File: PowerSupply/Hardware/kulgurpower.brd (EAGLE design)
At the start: 102 x 86.5 mm, 97 parts, among them X2 1727036

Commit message: Lot of changes to schematics. A lot.
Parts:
- removed E-STOP: PC-6-16/2-G-10.16-1913646, phoenix-1016:PC-6-16/2-G-10.16
- removed PWR1, PWR2, PWR3, PWR4: MST2V, con-phoenix-508:MSTBV2
- removed R10, R14, R3, R5: 100k, rcl:R0603
- removed R4: 680k, rcl:R0603
- removed SV2: (no value), con-lstb:MA20-2
- removed TP13: TPB2,54, testpad:B2,54
- added C22, C23, C24, C25, C26, C27, C28: 0.1, rcl:C0603
- added D1, D3: BAT54C, diode:SOT23
- added M1, M2, M3, M4: MST2V, con-phoenix-508:MSTBV2
- added R11, R15, R17, R19: 680k, rcl:R0603
- added R13, R16, R20: 100k, rcl:R0603
- added SV1: (no value), con-lstb:MA17-2
- added U$20, U$21, U$22, U$23, U$24, U$25, U$26: MAX1614EUA, MAX1614EUA:MAX1614EUA
- added U$27: PC-6-16/2-G-10.16-1913646, phoenix-1016:PC-6-16/2-G-10.16
- C12, C19, C6: device resistor:C0603@1 -> rcl:C0603
- C2: value 0.1 -> 47uF / 10V; device rcl:C0603 -> rcl:C/6032-28R
- C9: device resistor:C0603 -> rcl:C0603
- F1, F10, F2, F3, F4, F5, F6, F7, F8, F9: value PTCSMD -> 10A FUSE 1206
- U$1, U$10, U$12, U$14, U$15, U$2, U$3, U$5, U$6, U$7, U$9: value FDMS8558S -> AON6500
- moved R18 42.9 mm to (59.5, 11.4), turned to 270 degrees
- moved D20 21.0 mm to (94.3, 28.4)
- moved C2 10.8 mm to (33.2, 35.4), turned to 90 degrees
- moved U$2 7.25 mm to (75.0, 26.0)
- moved U$5 7.25 mm to (15.0, 26.0)
- moved U$6 7.25 mm to (55.1, 26.0)
- moved U$9 7.25 mm to (35.0, 26.0)
- moved U$10 6.50 mm to (35.0, 19.2)
- moved U$12 6.50 mm to (15.0, 19.2)
- moved U$3 6.50 mm to (75.0, 19.2)
- moved U$7 6.50 mm to (55.1, 19.2)
- moved PWRLED 6.40 mm to (85.1, 6.10)
- moved R12 6.40 mm to (85.1, 9.76)
- moved C21 6.04 mm to (23.2, 32.0), turned to 90 degrees
- moved F9 6.00 mm to (54.1, 67.8), flipped to the bottom
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- renumbered PWR5 to PC, PWR6 to MISC
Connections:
- removed net EN_OUT1: SV2.16, U$1.P$4
- removed net EN_OUT2: SV2.26, U$14.P$4
- removed net EN_OUT3: SV2.36, U$15.P$4
- removed net N$18 (its old number): L2.1, TP5.TP, U$17.P$4A
- removed net N$2 (its old number): L1.1, TP8.TP, U$16.P$4A
- removed net N$23 (its old number): L3.1, TP10.TP, U$18.P$4A
- removed net N$26: L4.1, TP15.TP, U$19.P$4A
- removed net PBUS1: F10.1, F7.1, F8.1, F9.1, U$1.P$1, U$1.P$2, U$1.P$3
- removed net PBUS2: F1.1, U$14.P$1, U$14.P$2, U$14.P$3
- removed net PBUS3: F2.1, U$15.P$1, U$15.P$2, U$15.P$3
- removed net SKIP0: SV2.8
- removed net SKIP1: SV2.18
- removed net SKIP2: SV2.28
- removed net SKIP3: SV2.38
- removed net V18V_AD: C2.1, R3.2, R4.2, SV2.6, TP13.TP
- removed net VBB0: C19.1, R18.1, SV2.2, U$12.P$5, U$12.P$6, U$12.P$7, U$12.P$8, U$5.P$5, U$5.P$6, U$5.P$7, U$5.P$8
- removed net VBB1: C12.1, R14.1, SV2.12, U$10.P$5, U$10.P$6, U$10.P$7, U$10.P$8, U$9.P$5, U$9.P$6, U$9.P$7, U$9.P$8
- removed net VBB2: C6.1, R10.1, SV2.22, U$6.P$5, U$6.P$6, U$6.P$7, U$6.P$8, U$7.P$5, U$7.P$6, U$7.P$7, U$7.P$8
- removed net VBB3: C9.1, R5.1, SV2.32, U$2.P$5, U$2.P$6, U$2.P$7, U$2.P$8, U$3.P$5, U$3.P$6, U$3.P$7, U$3.P$8
- new net !OFF_0: U$20.2, U$20.3
- new net !OFF_1: U$22.2, U$22.3
- new net !OFF_2: U$21.2, U$21.3
- new net !OFF_3: U$23.2, U$23.3
- new net BAT0_G: C19.2, U$12.P$4, U$20.6, U$5.P$4
- new net BAT0_S: C19.1, U$12.P$1, U$12.P$2, U$12.P$3, U$20.7, U$5.P$1, U$5.P$2, U$5.P$3
- new net BAT1_G: C12.2, U$10.P$4, U$22.6, U$9.P$4
- new net BAT1_S: C12.1, U$10.P$1, U$10.P$2, U$10.P$3, U$22.7, U$9.P$1, U$9.P$2, U$9.P$3
- new net BAT2_G: C6.2, U$21.6, U$6.P$4, U$7.P$4
- new net BAT2_S: C6.1, U$21.7, U$6.P$1, U$6.P$2, U$6.P$3, U$7.P$1, U$7.P$2, U$7.P$3
- new net BAT3_G: C9.2, U$2.P$4, U$23.6, U$3.P$4
- new net BAT3_S: C9.1, U$2.P$1, U$2.P$2, U$2.P$3, U$23.7, U$3.P$1, U$3.P$2, U$3.P$3
- new net LBI0: R11.1, R13.2, U$20.4
- new net LBI1: R15.1, R16.2, U$22.4
- new net LBI2: R17.1, R18.2, U$21.4
- new net LBI3: R19.1, R20.2, U$23.4
- new net OUT1_EN: SV1.20, U$24.1
- new net OUT1_G: C24.2, U$1.P$4, U$24.6
- new net OUT1_S: C24.1, F10.1, F7.1, F8.1, F9.1, U$1.P$1, U$1.P$2, U$1.P$3, U$24.7
- new net OUT2_EN: SV1.22, U$25.1
- new net OUT2_G: C22.2, U$14.P$4, U$25.6
- new net OUT2_S: C22.1, F1.1, U$14.P$1, U$14.P$2, U$14.P$3, U$25.7
- new net OUT3_EN: SV1.24, U$26.1
- new net OUT3_G: C23.2, U$15.P$4, U$26.6
- new net OUT3_S: C23.1, F2.1, U$15.P$1, U$15.P$2, U$15.P$3, U$26.7
- new net VSW0: L1.1, TP8.TP, U$16.P$4A, U$16.P$4B, U$16.P$4C, U$16.P$4D, U$16.P$4E, U$16.P$4F
- new net VSW1: L2.1, TP5.TP, U$17.P$4A, U$17.P$4B, U$17.P$4C, U$17.P$4D, U$17.P$4E, U$17.P$4F
- new net VSW2: L3.1, TP10.TP, U$18.P$4A, U$18.P$4B, U$18.P$4C, U$18.P$4D, U$18.P$4E, U$18.P$4F
- new net VSW3: L4.1, TP15.TP, U$19.P$4A, U$19.P$4B, U$19.P$4C, U$19.P$4D, U$19.P$4E, U$19.P$4F
- net !SKIP0: now also SV1.2
- net !SKIP1: now also SV1.6
- net !SKIP2: now also SV1.10
- net !SKIP3: now also SV1.14
- net +19V: now also D1.3, D3.3, SV1.34, U$16.P$5B, U$16.P$5C, U$16.P$5D, U$16.P$5E, U$16.P$5F, U$17.P$5B, U$17.P$5C, U$17.P$5D, U$17.P$5E, U$17.P$5F, U$18.P$5B, U$18.P$5C, U$18.P$5D, U$18.P$5E, U$18.P$5F, U$19.P$5B, U$19.P$5C, U$19.P$5D, U$19.P$5E, U$19.P$5F; no longer R4.1
- net 5V: now also C2.+, C25.2, C26.2, C27.2, C28.2, SV1.17; no longer SV2.15, SV2.25, SV2.35, SV2.5
- net BAT-: now also U$27.P$4, U$27.P$5, U$27.P$6; no longer E-STOP.P$4
- net BAT0_EN: now also D1.1, SV1.19, U$20.1; no longer C19.2, R18.2, SV2.1, U$12.P$4, U$5.P$4
- net BAT1_EN: now also D1.2, SV1.23, U$22.1; no longer C12.2, R14.2, SV2.11, U$10.P$4, U$9.P$4
- net BAT2_EN: now also D3.1, SV1.27, U$21.1; no longer C6.2, R10.2, SV2.21, U$6.P$4, U$7.P$4
- net BAT3_EN: now also D3.2, SV1.31, U$23.1; no longer C9.2, R5.2, SV2.31, U$2.P$4, U$3.P$4
- net GND: now also C2.-, C25.1, C26.1, C27.1, C28.1, M1.2, M2.2, M3.2, M4.2, R13.1, R16.1, R18.1, R20.1, SV1.11, SV1.12, SV1.15, SV1.16, SV1.3, SV1.4, SV1.7, SV1.8, U$20.5, U$21.5, U$22.5, U$23.5, U$24.2, U$24.4, U$24.5, U$25.2, U$25.4, U$25.5, U$26.2, U$26.4, U$26.5, U$27.P$1, U$27.P$2, U$27.P$3; no longer C2.2, E-STOP.P$1, PWR1.2, PWR2.2, PWR3.2, PWR4.2, R3.1, SV2.10, SV2.19, SV2.20, SV2.29, SV2.30, SV2.39, SV2.40, SV2.9
- net IBAT0_AD: now also SV1.1; no longer SV2.7
- net IBAT1_AD: now also SV1.5; no longer SV2.17
- net IBAT2_AD: now also SV1.9; no longer SV2.27
- net IBAT3_AD: now also SV1.13; no longer SV2.37
- net PWM0: now also SV1.26; no longer SV2.4
- net PWM1: now also SV1.28; no longer SV2.14
- net PWM2: now also SV1.30; no longer SV2.24
- net PWM3: now also SV1.32; no longer SV2.34
- net PWR1: now also M1.1; no longer PWR1.1
- net PWR2: now also M2.1; no longer PWR2.1
- net PWR3: now also M3.1; no longer PWR3.1
- net PWR4: now also M4.1; no longer PWR4.1
- net V+: now also U$2.P$5, U$2.P$6, U$2.P$7, U$2.P$8, U$24.8, U$25.8, U$26.8, U$5.P$5, U$5.P$6, U$5.P$7, U$5.P$8, U$6.P$5, U$6.P$6, U$6.P$7, U$6.P$8, U$9.P$5, U$9.P$6, U$9.P$7, U$9.P$8; no longer U$10.P$1, U$10.P$2, U$10.P$3, U$12.P$1, U$12.P$2, U$12.P$3, U$3.P$1, U$3.P$2, U$3.P$3, U$7.P$1, U$7.P$2, U$7.P$3
- net VBAT0: now also SV1.21; no longer SV2.3
- net VBAT0_X: now also R11.2, U$12.P$5, U$12.P$6, U$12.P$7, U$12.P$8, U$20.8; no longer U$5.P$1, U$5.P$2, U$5.P$3
- net VBAT1: now also SV1.25; no longer SV2.13
- net VBAT1_X: now also R15.2, U$10.P$5, U$10.P$6, U$10.P$7, U$10.P$8, U$22.8; no longer U$9.P$1, U$9.P$2, U$9.P$3
- net VBAT2: now also SV1.29; no longer SV2.23
- net VBAT2_X: now also R17.2, U$21.8, U$7.P$5, U$7.P$6, U$7.P$7, U$7.P$8; no longer U$6.P$1, U$6.P$2, U$6.P$3
- net VBAT3: now also SV1.33; no longer SV2.33
- net VBAT3_X: now also R19.2, U$23.8, U$3.P$5, U$3.P$6, U$3.P$7, U$3.P$8; no longer U$2.P$1, U$2.P$2, U$2.P$3
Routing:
- net GND: track 507.1 -> 178.0 mm, vias 1 -> 36
- net V+: track 160.9 -> 48.6 mm, vias 5 -> 4
- net !SKIP3: track 0.00 -> 66.0 mm, vias 0 -> 1
- net OUT3_EN: track 0.00 -> 53.4 mm, vias 0 -> 1
- net !SKIP2: track 0.00 -> 52.0 mm, vias 0 -> 2
- net +19V: track 113.8 -> 160.7 mm, vias 4 -> 6
- net EN_OUT2: track 46.0 -> 0.00 mm, vias 1 -> 0
- net VBB3: track 45.5 -> 0.00 mm, vias 1 -> 0
- net OUT2_EN: track 0.00 -> 44.8 mm, vias 0 -> 1
- net VBB2: track 43.7 -> 0.00 mm, vias 1 -> 0
- net EN_OUT3: track 42.4 -> 0.00 mm, vias 1 -> 0
- net EN_OUT1: track 42.1 -> 0.00 mm
- net VBB1: track 38.6 -> 0.00 mm, vias 1 -> 0
- net 5V: track 203.0 -> 166.1 mm, vias 1 -> 15
- net !SKIP1: track 0.00 -> 35.9 mm, vias 0 -> 1
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- added copper zone on layer 16, net BAT0_S
- added copper zone on layer 16, net BAT1_S
- added copper zone on layer 16, net BAT2_S
- added copper zone on layer 16, net BAT3_S
- added copper zone on layer 1, net GND
- added copper zone on layer 16, net GND
- added copper zone on layer 16, net OUT1_S
- added copper zone on layer 16, net OUT2_S
- added copper zone on layer 16, net OUT3_S
- added copper zone on layer 16, net PWR1
- added copper zone on layer 16, net PWR2
- added copper zone on layer 16, net PWR3
- added copper zone on layer 16, net PWR4
- added copper zone on layer 16, net PWR5
- added copper zone on layer 16, net PWR6
- added copper zone on layer 16, net V+
- added copper zone on layer 16, net VBAT0
- added copper zone on layer 16, net VBAT0_X
- added copper zone on layer 16, net VBAT1
- added copper zone on layer 16, net VBAT1_X
- added copper zone on layer 16, net VBAT2
- added copper zone on layer 16, net VBAT2_X
- added copper zone on layer 16, net VBAT3
- added copper zone on layer 16, net VBAT3_X
- added copper zone on layer 16, net VSW0
- added copper zone on layer 16, net VSW1
- added copper zone on layer 16, net VSW2
- added copper zone on layer 16, net VSW3
- removed copper zone on layer 1, net PBUS1
- removed copper zone on layer 1, net PBUS2
- removed copper zone on layer 1, net PBUS3
- removed copper zone on layer 1, net PWR1
- removed copper zone on layer 1, net PWR2
- removed copper zone on layer 1, net PWR3
- removed copper zone on layer 1, net PWR4
- removed copper zone on layer 1, net PWR5
- removed copper zone on layer 1, net PWR6
- removed copper zone on layer 16, net VBB0
- removed copper zone on layer 16, net VBB1
- removed copper zone on layer 16, net VBB2
- removed copper zone on layer 16, net VBB3

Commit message: lot of work done on schematics
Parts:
- removed L3, L4: 4,7uH, inductors:DR73
- removed SV1: (no value), con-lstb:MA17-2
- removed TP10, TP15, TP5, TP8: TPB2,54, testpad:B2,54
- removed U$16, U$18, U$19: CSD97374Q4M, CSD97374Q4M:CSD97374Q4M
- added C104, C113, C32: 220n, rcl:C0603
- added C29: 0,1u, rcl:C0603
- added C30: (no value), rcl:C/6032-28R
- added C33, C34: 100pF, SparkFun:0805
- added R10, R14, R25, R33: 100k, rcl:R0603
- added R21: 120k, rcl:R0603
- added R23: 18k, rcl:R0603
- added R3: 300k, rcl:R0603
- added R31, R32: 3k16, rcl:R0603
- added R39, R4, R5: 30k, rcl:R0603
- added R40: 270k, rcl:R0603
- added SJ100, SJ104, SJ108, SJ110, SJ114: 0R, rcl:R0603
- added U$105, U$106, U$107, U$108: IRF8252, tonu:SO8
- added X1: 1727036, con-phoenix-3.81:1727036
- added X3, X4: 22-23-2031, con-molex:22-23-2031
- added X5: 22-23-2021, con-molex:22-23-2021
- C1, C13, C14, C15, C3: value 0.1 -> (none); device rcl:C0603 -> rcl:C/6032-28R
- C10: value 0.1 -> 220n
- C16, C20, C21, C8: value 0.1 -> 0,1u
- C17: value 0.1 -> 10uF/6.3V; device rcl:C0603 -> rcl:C1210
- C2: value 47uF / 10V -> (none)
- C5: value 0.1 -> 10u; device rcl:C0603 -> rcl:C1210
- U$17: value CSD97374Q4M -> TPS51222RTVT; device CSD97374Q4M:CSD97374Q4M -> tps51222:QFN-32
- X2: value 1727036 -> 2534-; device con-phoenix-3.81:1727036 -> con-3m:PAK100/2500-34
- moved C1 74.2 mm to (99.0, 23.5), flipped to the top, turned to 270 degrees
- moved L1 73.7 mm to (97.5, 15.0), flipped to the top, turned to 180 degrees
- moved X2 71.3 mm to (33.5, 43.0), turned to 0 degrees
- moved C21 63.1 mm to (85.7, 24.1), flipped to the top, turned to 180 degrees
- moved C3 61.2 mm to (88.0, 12.5), flipped to the top, turned to 180 degrees
- moved C5 46.8 mm to (88.0, 20.3), flipped to the top
- moved C8 46.1 mm to (90.4, 24.1), flipped to the top, turned to 0 degrees
- moved C2 45.4 mm to (77.0, 23.5), flipped to the top, turned to 270 degrees
- moved U$17 44.6 mm to (88.1, 29.1), flipped to the top, turned to 90 degrees
- moved C13 38.8 mm to (97.5, 15.0)
- moved U$23 38.6 mm to (47.8, 22.5), flipped to the top, turned to 90 degrees
- moved R19 37.0 mm to (48.8, 27.5), flipped to the top, turned to 180 degrees
- moved L2 35.6 mm to (78.5, 15.0), flipped to the top, turned to 180 degrees
- moved C10 35.5 mm to (81.6, 35.4), flipped to the top, turned to 180 degrees
- moved D20 34.8 mm to (59.8, 23.9)
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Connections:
- removed net !SKIP0: SV1.2, U$16.P$1
- removed net !SKIP1: SV1.6, U$17.P$1
- removed net !SKIP2: SV1.10, U$18.P$1
- removed net !SKIP3: SV1.14, U$19.P$1
- removed net N$2: C8.1, U$17.P$7
- removed net N$20: C17.2, U$19.P$6
- removed net N$22: C1.2, U$16.P$6
- removed net N$23: C14.1, U$18.P$7
- removed net N$3: C8.2, U$17.P$6
- removed net PWM0: SV1.26, U$16.P$8
- removed net PWM1: SV1.28, U$17.P$8
- removed net PWM2: SV1.30, U$18.P$8
- removed net PWM3: SV1.32, U$19.P$8
- removed net VSW0: L1.1, TP8.TP, U$16.P$4A, U$16.P$4B, U$16.P$4C, U$16.P$4D, U$16.P$4E, U$16.P$4F
- removed net VSW1: L2.1, TP5.TP, U$17.P$4A, U$17.P$4B, U$17.P$4C, U$17.P$4D, U$17.P$4E, U$17.P$4F
- removed net VSW2: L3.1, TP10.TP, U$18.P$4A, U$18.P$4B, U$18.P$4C, U$18.P$4D, U$18.P$4E, U$18.P$4F
- removed net VSW3: L4.1, TP15.TP, U$19.P$4A, U$19.P$4B, U$19.P$4C, U$19.P$4D, U$19.P$4E, U$19.P$4F
- new net +5V: C1.+, C113.1, C13.+, L1.1, SJ114.2, X1.1
- new net COMP1: C34.1, R23.1, U$17.P$10
- new net COMP2: C33.1, R39.2, U$17.P$15
- new net COMPUTER_PWR: X2.28, X5.2
- new net CSN1: C16.1, R21.2, R25.2, SJ114.1, U$17.P$2, U$17.P$8
- new net CSN2: C20.1, R33.1, R40.2, SJ100.1, U$17.P$17
- new net CSP1: C16.2, R25.1, R31.1, U$17.P$7
- new net CSP2: C20.2, R32.1, R33.2, U$17.P$18
- new net DRVH1: U$105.4, U$17.P$1
- new net DRVH2: U$108.4, U$17.P$24
- new net DRVL1: U$106.4, U$17.P$30
- new net DRVL2: U$107.4, U$17.P$27
- new net ENABLE_PWR: U$17.P$12, X2.30
- new net IMON1: U$17.P$11, X2.27
- new net IMON2: U$17.P$14, X2.29
- new net N$29: C8.1, U$17.P$31
- new net N$30: C21.1, U$17.P$26
- new net OUT4_EN: U$17.P$4, X2.24
- new net OUT5_EN: U$17.P$21, X2.26
- new net PGOOD1: R10.2, U$17.P$5, X2.31
- new net PGOOD2: R14.2, U$17.P$20, X2.33
- new net PWM_A: X2.34, X3.3
- new net PWM_B: X2.32, X4.3
- new net SERVO: C104.1, C14.+, C15.+, C2.+, C30.+, L2.2, SJ100.2, X1.3, X3.2, X4.2
- new net SW1: C8.2, R31.2, SJ108.1, U$17.P$32
- new net SW2: C21.2, R32.2, SJ110.1, U$17.P$25
- new net VIN: SJ104.1, U$17.P$23
- new net VREF2: C10.1, C33.2, C34.2, R23.2, R39.1, U$17.P$13, U$17.P$19, U$17.P$6
- new net VREG3: C17.2, R10.1, R14.1, U$17.P$22
- new net X1: L1.2, SJ108.2, U$105.1, U$105.2, U$105.3, U$106.5, U$106.6, U$106.7, U$106.8
- new net X2: L2.1, SJ110.2, U$107.5, U$107.6, U$107.7, U$107.8, U$108.1, U$108.2, U$108.3
- net +19V: now also X2.14, X2.16; no longer C13.1, C16.1, C21.1, C5.1, SV1.34, U$16.P$5A, U$16.P$5B, U$16.P$5C, U$16.P$5D, U$16.P$5E, U$16.P$5F, U$17.P$5A, U$17.P$5B, U$17.P$5C, U$17.P$5D, U$17.P$5E, U$17.P$5F, U$18.P$5A, U$18.P$5B, U$18.P$5C, U$18.P$5D, U$18.P$5E, U$18.P$5F, U$19.P$5A, U$19.P$5B, U$19.P$5C, U$19.P$5D, U$19.P$5E, U$19.P$5F, X2.1
- net 5V: now also C5.2, U$17.P$29; no longer C10.1, C15.1, C2.+, C20.1, C3.1, SV1.17, U$16.P$2, U$17.P$2, U$18.P$2, U$19.P$2
- net BAT0_EN: now also X2.9; no longer SV1.19
- net BAT1_EN: now also X2.11; no longer SV1.23
- net BAT2_EN: now also X2.13; no longer SV1.27
- net BAT3_EN: now also X2.15; no longer SV1.31
- net GND: now also C1.-, C104.2, C113.2, C13.-, C14.-, C15.-, C17.1, C29.1, C3.-, C30.-, C32.2, C5.1, R3.1, R4.1, R5.1, U$106.1, U$106.2, U$106.3, U$107.1, U$107.2, U$107.3, U$17.P$28, U$17.P$33, X1.2, X1.4, X2.10, X2.17, X3.1, X4.1, X5.1; no longer C13.2, C15.2, C16.2, C20.2, C21.2, C3.2, C5.2, SV1.11, SV1.12, SV1.15, SV1.16, SV1.3, SV1.4, SV1.7, SV1.8, U$16.P$3, U$16.PAD@1, U$17.P$3, U$17.PAD@1, U$18.P$3, U$18.PAD@1, U$19.P$3, U$19.PAD@1, X2.2
- net IBAT0_AD: now also X2.19; no longer SV1.1
- net IBAT1_AD: now also X2.21; no longer SV1.5
- net IBAT2_AD: now also X2.23; no longer SV1.9
- net IBAT3_AD: now also X2.25; no longer SV1.13
- net N$18: now also R40.1, R5.2, U$17.P$16; no longer C17.1, U$19.P$7
- net N$24: now also R3.2, U$17.P$3; no longer C14.2, U$18.P$6
- net N$5: now also R21.1, R4.2, U$17.P$9; no longer C1.1, U$16.P$7
- net OUT1_EN: now also X2.18; no longer SV1.20
- net OUT2_EN: now also X2.20; no longer SV1.22
- net OUT3_EN: now also X2.22; no longer SV1.24
- net V+: now also C29.2, C3.+, C32.1, SJ104.2, U$105.5, U$105.6, U$105.7, U$105.8, U$108.5, U$108.6, U$108.7, U$108.8, X2.12
- net VBAT0: now also X2.1, X2.2; no longer SV1.21
- net VBAT0_X: no longer L1.2
- net VBAT1: now also X2.3, X2.4; no longer SV1.25
- net VBAT1_X: no longer L2.2
- net VBAT2: now also X2.5, X2.6; no longer SV1.29
- net VBAT2_X: no longer L3.2
- net VBAT3: now also X2.7, X2.8; no longer SV1.33
- net VBAT3_X: no longer L4.2
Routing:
- net +19V: track 160.7 -> 16.8 mm, vias 6 -> 2
- net GND: track 178.0 -> 53.4 mm, vias 36 -> 18
- net !SKIP3: track 66.0 -> 0.00 mm, vias 1 -> 0
- net 5V: track 166.1 -> 103.5 mm, vias 15 -> 5
- net OUT4_EN: track 0.00 -> 59.5 mm, vias 0 -> 1
- net SERVO: track 0.00 -> 56.1 mm, vias 0 -> 2
- net !SKIP2: track 52.0 -> 0.00 mm, vias 2 -> 0
- net OUT5_EN: track 0.00 -> 48.6 mm, vias 0 -> 2
- net COMPUTER_PWR: track 0.00 -> 48.4 mm
- net IMON1: track 0.00 -> 47.6 mm, vias 0 -> 2
- net PGOOD1: track 0.00 -> 46.5 mm, vias 0 -> 2
- net ENABLE_PWR: track 0.00 -> 46.2 mm, vias 0 -> 1
- net PWM_A: track 0.00 -> 45.4 mm
- net PWM3: track 45.0 -> 0.00 mm, vias 2 -> 0
- net IMON2: track 0.00 -> 43.9 mm, vias 0 -> 2
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- added copper zone on layer 16, net X1
- added copper zone on layer 16, net X2
- removed copper zone on layer 16, net VSW0
- removed copper zone on layer 16, net VSW1
- removed copper zone on layer 16, net VSW2
- removed copper zone on layer 16, net VSW3

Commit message: More work on electronics
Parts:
- moved C22 0.24 mm to (75.7, 48.6)
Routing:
- net VREG3: track 9.13 -> 19.6 mm, vias 2 -> 3
- net +5V: track 26.1 -> 30.6 mm
- net GND: track 53.4 -> 57.1 mm, vias 18 -> 20
- net SERVO: track 56.1 -> 53.3 mm
- net VBAT1: track 38.5 -> 36.1 mm
- net BAT2_S: track 7.43 -> 5.24 mm
- net !OFF_3: track 2.66 -> 0.65 mm
- net OUT5_EN: track 48.6 -> 50.2 mm, vias 2 -> 1
- net VBAT2_X: track 16.6 -> 15.1 mm
- net N$17: track 5.00 -> 6.38 mm
- net OUT3_EN: track 57.9 -> 56.8 mm
- net PGOOD1: track 46.5 -> 45.4 mm, vias 2 -> 3
- net PGOOD2: track 36.9 -> 37.9 mm, vias 2 -> 3
- net N$18: track 6.43 -> 7.24 mm
- net V+: track 10.9 -> 10.3 mm
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
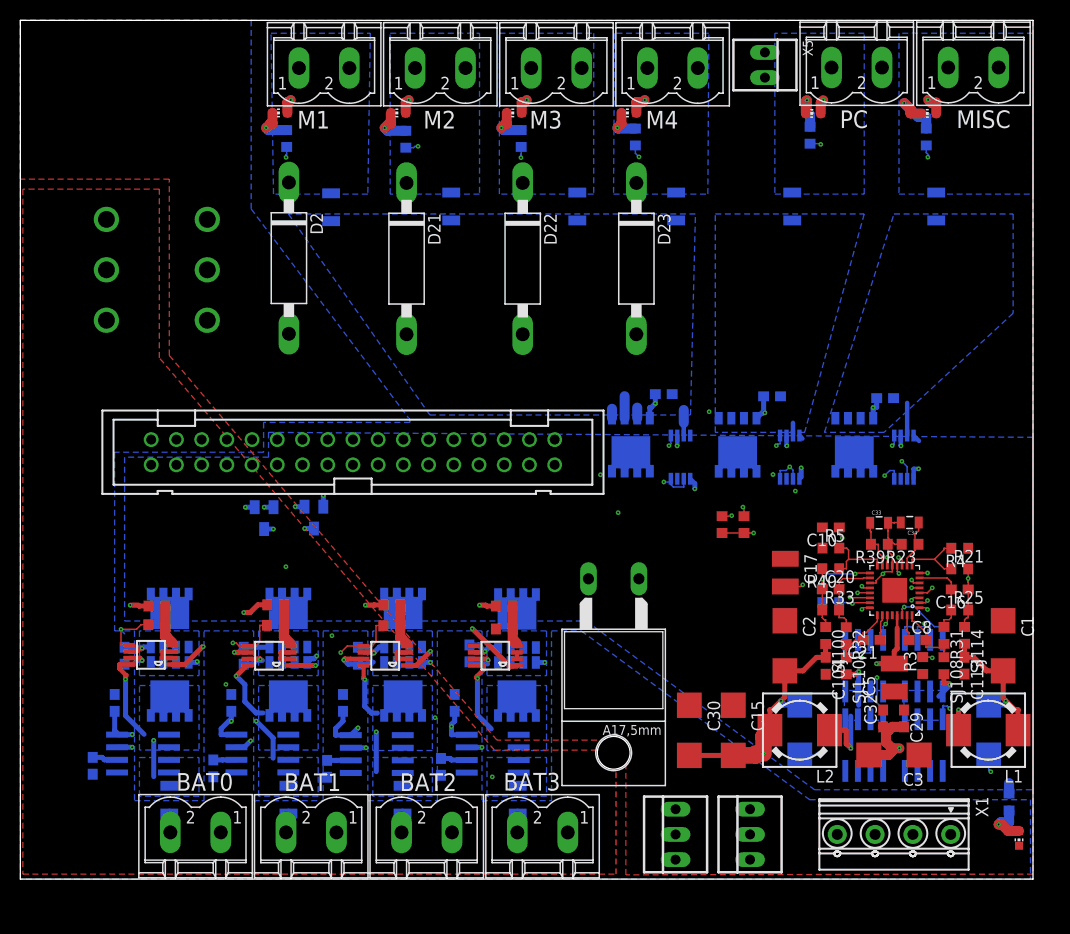
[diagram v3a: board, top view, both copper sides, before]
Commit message: Converted into 2 layer board from 4 layer. Seems to be OK for production
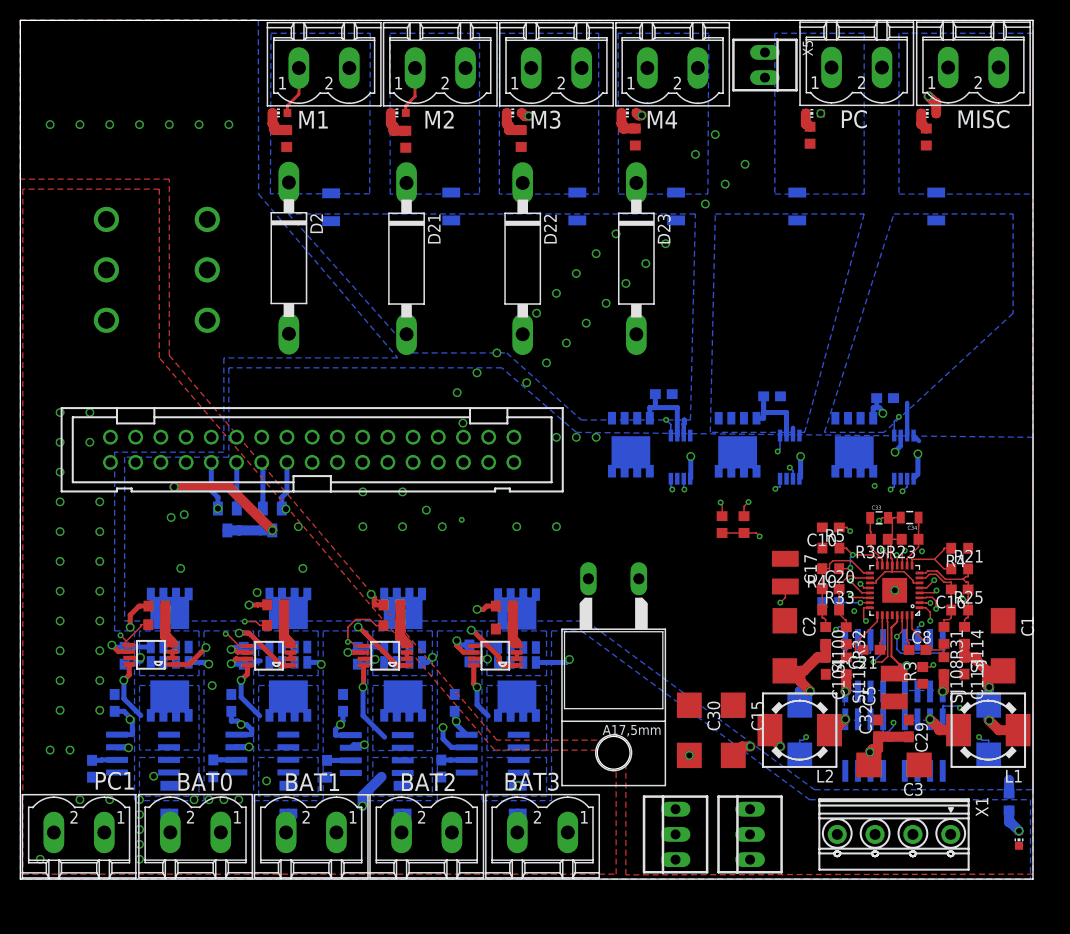
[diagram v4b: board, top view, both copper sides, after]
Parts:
- added PC1: MST2V, con-phoenix-508:MSTBV2
- moved D3 4.19 mm to (25.4, 36.2)
- moved X2 4.11 mm to (29.4, 43.2)
- moved D1 3.70 mm to (20.9, 36.2)
- moved C29 1.12 mm to (89.5, 15.2)
- moved C32 1.12 mm to (86.4, 15.2)
- moved C21 1.00 mm to (85.7, 23.1)
- moved C3 1.00 mm to (88.0, 11.5)
- moved C5 1.00 mm to (88.0, 19.3)
- moved C8 1.00 mm to (90.4, 23.1)
- moved R3 1.00 mm to (90.9, 20.5)
- moved C33 0.50 mm to (86.5, 36.4)
- moved C34 0.50 mm to (89.6, 36.4)
- moved F1 0.50 mm to (78.2, 67.8)
- moved R23 0.50 mm to (89.6, 34.2)
- moved R39 0.50 mm to (86.5, 34.2)
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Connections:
- net +19V: now also PC1.2
- net GND: now also PC1.1
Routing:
- net 5V: track 103.4 -> 25.2 mm
- net SERVO: track 53.3 -> 16.9 mm, vias 2 -> 4
- net VBAT3: track 45.5 -> 61.2 mm
- net VBAT2: track 40.7 -> 53.1 mm, vias 2 -> 3
- net BAT3_G: track 11.9 -> 22.6 mm
- net GND: track 57.1 -> 47.1 mm, vias 20 -> 60
- net PGOOD1: track 45.4 -> 55.0 mm
- net BAT3_EN: track 31.1 -> 40.1 mm, vias 2 -> 3
- net X2: track 11.7 -> 3.82 mm
- net BAT0_G: track 11.2 -> 18.7 mm
- net BAT2_EN: track 28.6 -> 36.1 mm
- net ENABLE_PWR: track 46.2 -> 52.4 mm, vias 1 -> 2
- net VBAT0: track 34.1 -> 40.0 mm
- net DRVL2: track 2.66 -> 8.53 mm
- net IMON1: track 47.7 -> 53.3 mm, vias 2 -> 1
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- added copper zone on layer 15, net +19V
- added copper zone on layer 15, net 5V
- added copper zone on layer 15, net BAT-
- added copper zone on layer 2, net BAT-
- added copper zone on layer 15, net GND
- added copper zone on layer 2, net GND
- added copper zone on layer 15, net PWR1
- added copper zone on layer 15, net PWR2
- added copper zone on layer 15, net PWR3
- added copper zone on layer 15, net PWR4
- added copper zone on layer 15, net SERVO

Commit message: Silkscreen fixes
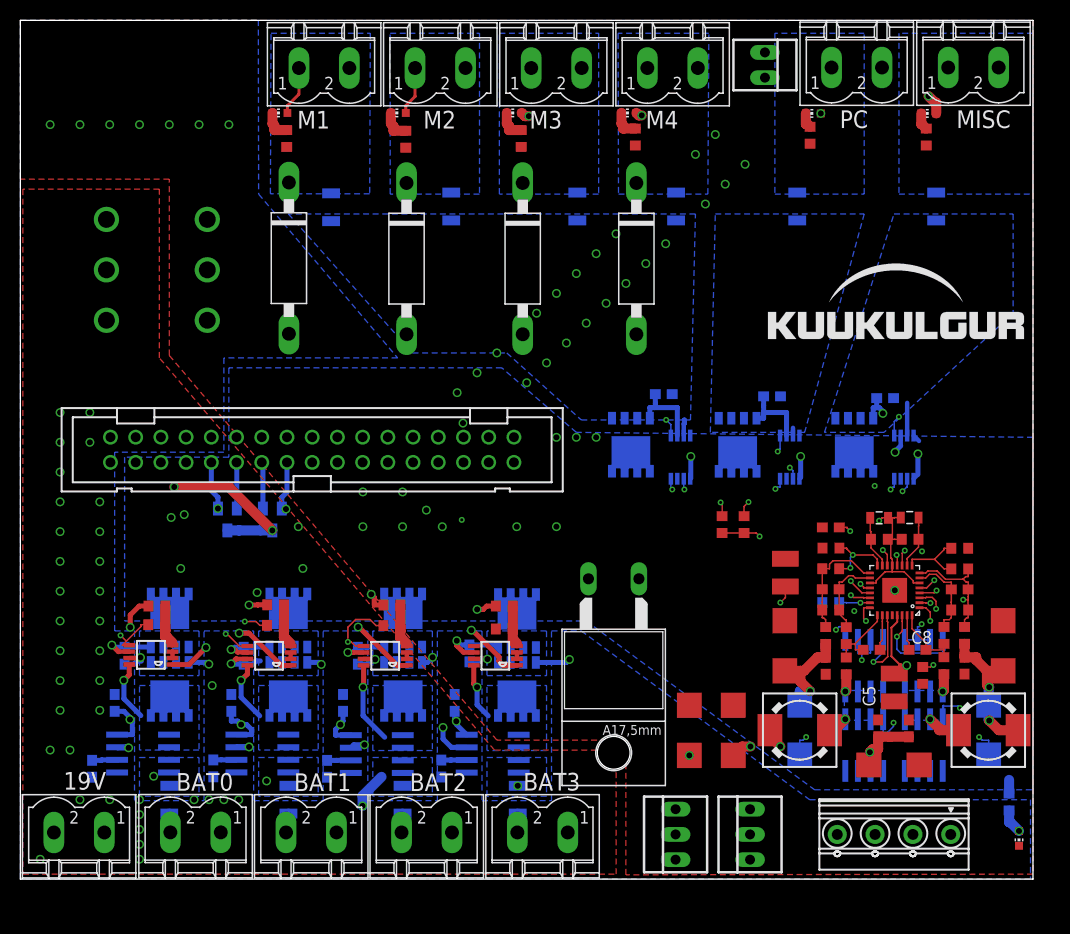
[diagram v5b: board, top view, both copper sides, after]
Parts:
- renumbered PC1 to 19V
